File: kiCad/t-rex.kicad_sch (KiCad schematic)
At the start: 123 parts, among them J0 Conn_01x03, SW0 MX, SW1 MX, SW10 MX, SW11 MX, SW12 MX, SW13 MX, SW14 MX, SW15 MX, SW16 MX, SW17 MX, SW18 MX, SW19 MX, SW2 MX, SW20 MX, SW21 MX, SW22 MX, SW23 MX, SW24 MX, SW25 MX, SW26 MX, SW27 MX, SW28 MX, SW29 MX, SW3 MX, SW30 MX, SW31 MX, SW32 MX, SW33 MX, SW34 MX, SW35 MX, SW36 MX, SW37 MX, SW38 MX, SW39 MX, SW4 MX, SW40 MX, SW41 MX, SW42 MX, SW43 MX, SW44 MX, SW45 MX, SW46 MX, SW47 MX, SW48 MX, SW49 MX, SW5 MX, SW50 MX, SW51 MX, SW52 MX, SW53 MX, SW54 MX, SW55 MX, SW56 MX, SW57 MX, SW58 MX, SW59 MX, SW6 MX, SW61 MX, SW7 MX, SW8 MX, SW9 MX, U0 Sparkfun_Pro_Micro

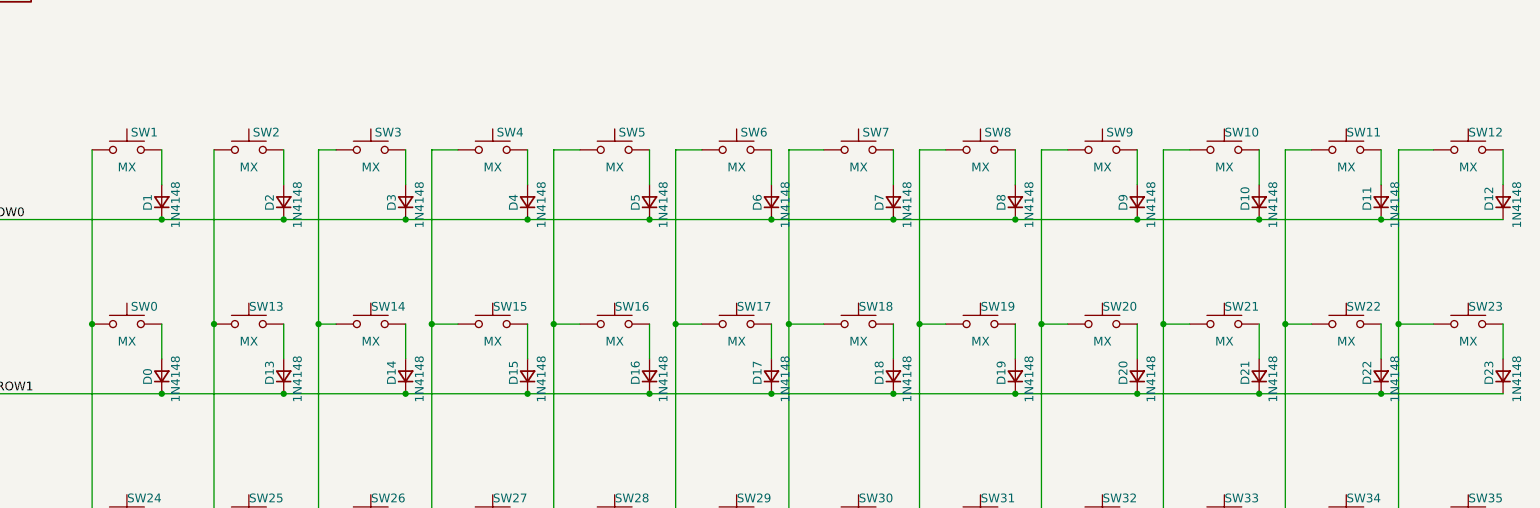
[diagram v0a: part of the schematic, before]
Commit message: add gerbers, fix labels
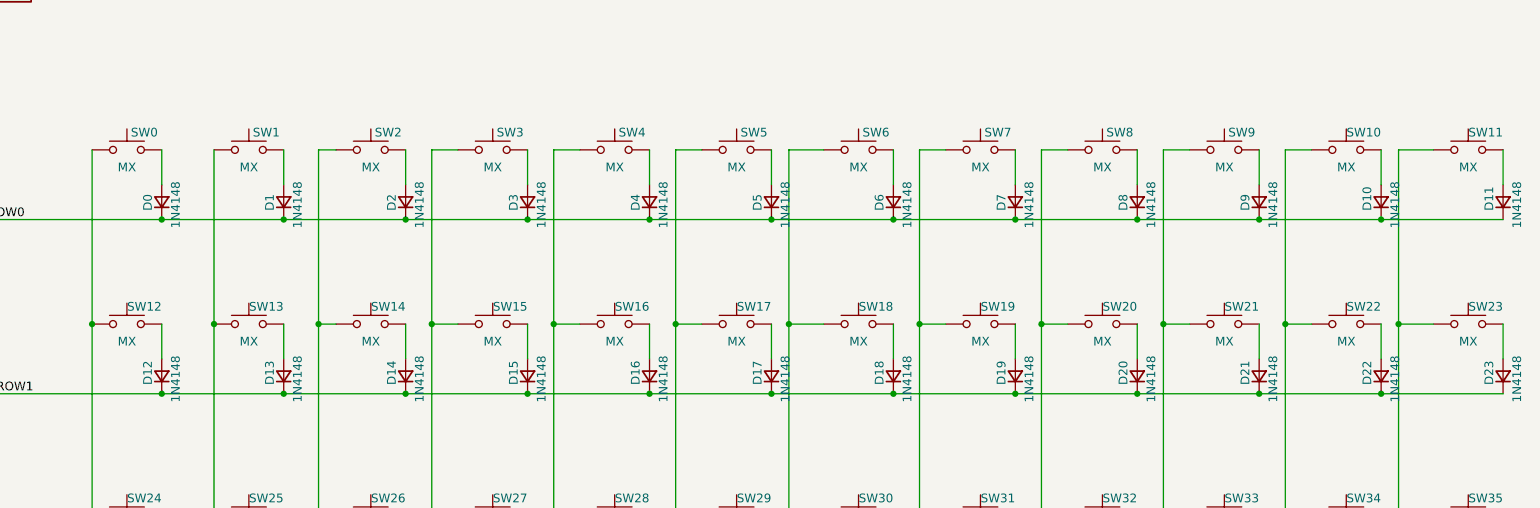
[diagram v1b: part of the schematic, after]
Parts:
- renumbered D1 to D0, D2 to D1, D11 to D10, D12 to D11, D0 to D12, D3 to D2, D4 to D3, D5 to D4, D6 to D5, D7 to D6, D8 to D7, D9 to D8, D10 to D9, SW1 to SW0, SW2 to SW1, SW11 to SW10, SW12 to SW11, SW0 to SW12, SW3 to SW2, SW4 to SW3, SW5 to SW4, SW6 to SW5, SW7 to SW6, SW8 to SW7, SW9 to SW8, SW10 to SW9
